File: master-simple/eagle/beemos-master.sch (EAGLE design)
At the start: 56 parts, among them CON1 BATTERY, CON2 JACK_DC_BARREL, CON3 SPI, IC1 32U4, IC2 MCP73831T, IC3 MCP1703CB, IC4 DMP1045U, J1 RJ12STRAIGHT-I2C, J2 RJ12STRAIGHT-I2C, J3 RJ12STRAIGHT-I2C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

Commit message: master: cleanup
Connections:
- net N$7: now also IC2.STAT
- net SCL: no longer R1.1
- net SDA: now also R1.1
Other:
- moved on the sheet: R1, R6
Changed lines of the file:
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@@
 <?xml version="1.0" encoding="utf-8"?>
 <!DOCTYPE eagle SYSTEM "eagle.dtd">
-<eagle version="9.0.0">
+<eagle version="8.7.1">
 <drawing>
 <settings>
@@
 <instance part="GND7" gate="1" x="45.72" y="167.64" rot="R180"/>
 <instance part="P+2" gate="G$1" x="73.66" y="215.9"/>
-<instance part="R1" gate="G$1" x="185.42" y="147.32" rot="R90"/>
-<instance part="R6" gate="G$1" x="193.04" y="147.32" rot="R90"/>
+<instance part="R1" gate="G$1" x="185.42" y="152.4" rot="R90"/>
+<instance part="R6" gate="G$1" x="193.04" y="152.4" rot="R90"/>
 <instance part="P+3" gate="G$1" x="96.52" y="200.66"/>
 <instance part="P+4" gate="G$1" x="106.68" y="205.74"/>
@@
 <attribute name="ELECROW" x="66.04" y="91.44" size="1.778" layer="96" display="off"/>
 </instance>
-<instance part="SUPPLY1" gate="G$1" x="195.58" y="157.48"/>
+<instance part="SUPPLY1" gate="G$1" x="195.58" y="162.56"/>
 <instance part="GND3" gate="1" x="238.76" y="86.36" rot="R270"/>
 <instance part="RT2" gate="G$1" x="236.22" y="96.52" rot="R180"/>
@@
 <wire x1="160.02" y1="208.28" x2="175.26" y2="208.28" width="0.1524" layer="91"/>
 <label x="170.18" y="208.28" size="1.778" layer="95"/>
+<junction x="160.02" y="208.28"/>
 </segment>
 </net>
@@
 <wire x1="160.02" y1="210.82" x2="175.26" y2="210.82" width="0.1524" layer="91"/>
 <label x="170.18" y="210.82" size="1.778" layer="95"/>
+<junction x="160.02" y="210.82"/>
 </segment>
 </net>
@@
 <wire x1="160.02" y1="213.36" x2="175.26" y2="213.36" width="0.1524" layer="91"/>
 <label x="170.18" y="213.36" size="1.778" layer="95"/>
+<junction x="160.02" y="213.36"/>
 </segment>
 </net>
@@
 <wire x1="160.02" y1="215.9" x2="175.26" y2="215.9" width="0.1524" layer="91"/>
 <label x="170.18" y="215.9" size="1.778" layer="95"/>
+<junction x="160.02" y="215.9"/>
 </segment>
 <segment>
@@
 <wire x1="160.02" y1="205.74" x2="175.26" y2="205.74" width="0.1524" layer="91"/>
 <label x="170.18" y="205.74" size="1.778" layer="95"/>
+<junction x="160.02" y="205.74"/>
 </segment>
 </net>
@@
 <segment>
 <pinref part="IC1" gate="G$1" pin="PD1(INT1/SDA)"/>
-<wire x1="160.02" y1="144.78" x2="175.26" y2="144.78" width="0.1524" layer="91"/>
+<wire x1="160.02" y1="144.78" x2="185.42" y2="144.78" width="0.1524" layer="91"/>
 <label x="170.18" y="144.78" size="1.778" layer="95"/>
+<pinref part="R1" gate="G$1" pin="1"/>
+<wire x1="185.42" y1="147.32" x2="185.42" y2="144.78" width="0.1524" layer="91"/>
 </segment>
 <segment>
@@
 <net name="SCL" class="0">
 <segment>
-<pinref part="IC1" gate="G$1" pin="PD0(INT0/OC0B/SCL)"/>
-<wire x1="160.02" y1="142.24" x2="185.42" y2="142.24" width="0.1524" layer="91"/>
-<label x="170.18" y="142.24" size="1.778" layer="95"/>
-<pinref part="R1" gate="G$1" pin="1"/>
-<pinref part="R6" gate="G$1" pin="1"/>
-<wire x1="193.04" y1="142.24" x2="185.42" y2="142.24" width="0.1524" layer="91"/>
-<junction x="185.42" y="142.24"/>
-</segment>
-<segment>
 <pinref part="U$1" gate="G$1" pin="SCL"/>
 <wire x1="27.94" y1="162.56" x2="45.72" y2="162.56" width="0.1524" layer="91"/>
@@
 <label x="91.44" y="27.94" size="1.778" layer="95"/>
 </segment>
+<segment>
+<pinref part="IC1" gate="G$1" pin="PD0(INT0/OC0B/SCL)"/>
+<pinref part="R6" gate="G$1" pin="1"/>
+<wire x1="160.02" y1="142.24" x2="193.04" y2="142.24" width="0.1524" layer="91"/>
+<wire x1="193.04" y1="142.24" x2="193.04" y2="147.32" width="0.1524" layer="91"/>
+<label x="170.18" y="142.24" size="1.778" layer="95"/>
+</segment>
 </net>
 <net name="TX" class="0">
@@
 <wire x1="160.02" y1="195.58" x2="175.26" y2="195.58" width="0.1524" layer="91"/>
 <label x="170.18" y="195.58" size="1.778" layer="95"/>
+<junction x="160.02" y="195.58"/>
 </segment>
 <segment>
@@
 <wire x1="160.02" y1="203.2" x2="175.26" y2="203.2" width="0.1524" layer="91"/>
 <label x="170.18" y="203.2" size="1.778" layer="95"/>
+<junction x="160.02" y="203.2"/>
 </segment>
 </net>
@@
 <wire x1="160.02" y1="198.12" x2="175.26" y2="198.12" width="0.1524" layer="91"/>
 <label x="170.18" y="198.12" size="1.778" layer="95"/>
+<junction x="160.02" y="198.12"/>
 </segment>
 </net>
@@
 <pinref part="R1" gate="G$1" pin="2"/>
 <pinref part="R6" gate="G$1" pin="2"/>
-<wire x1="185.42" y1="152.4" x2="193.04" y2="152.4" width="0.1524" layer="91"/>
-<wire x1="193.04" y1="152.4" x2="195.58" y2="152.4" width="0.1524" layer="91"/>
+<wire x1="185.42" y1="157.48" x2="193.04" y2="157.48" width="0.1524" layer="91"/>
+<wire x1="193.04" y1="157.48" x2="195.58" y2="157.48" width="0.1524" layer="91"/>
 <pinref part="SUPPLY1" gate="G$1" pin="VDD"/>
-<wire x1="195.58" y1="154.94" x2="195.58" y2="152.4" width="0.1524" layer="91"/>
-<junction x="193.04" y="152.4"/>
+<wire x1="195.58" y1="160.02" x2="195.58" y2="157.48" width="0.1524" layer="91"/>
+<junction x="193.04" y="157.48"/>
 </segment>
 </net>
@@
 <pinref part="R16" gate="G$1" pin="2"/>
 <wire x1="71.12" y1="91.44" x2="73.66" y2="91.44" width="0.1524" layer="91"/>
-</segment>
-</net>
+<pinref part="IC2" gate="G$1" pin="STAT"/>
+<junction x="73.66" y="91.44"/>
+</segment>
+</net>

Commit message: Arranged labels and resistors in beemos master board layout
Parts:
- D4: value ||Schottky -> Schottky||
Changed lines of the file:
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@@
 <?xml version="1.0" encoding="utf-8"?>
 <!DOCTYPE eagle SYSTEM "eagle.dtd">
-<eagle version="8.7.1">
+<eagle version="9.0.0">
 <drawing>
 <settings>
@@
 <part name="J4" library="lpatiny" deviceset="RJ12" device="STRAIGHT-I2C" value="RJ12STRAIGHT-I2C"/>
 <part name="CON2" library="lpatiny" deviceset="JACK_DC_BARREL" device=""/>
-<part name="D4" library="diode" library_urn="urn:adsk.eagle:library:210" deviceset="MBR0520LT" device="" package3d_urn="urn:adsk.eagle:package:43420/1" value="||Schottky">
+<part name="D4" library="diode" library_urn="urn:adsk.eagle:library:210" deviceset="MBR0520LT" device="" package3d_urn="urn:adsk.eagle:package:43420/1" value="Schottky||">
 <attribute name="LCSC" value="C82544"/>
 <attribute name="MPN" value="621-1N5819HW-F"/>

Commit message: Added power/com LEDs, extra pins exposed, cristal symmetric
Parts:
- added LED1: red, led:LEDCHIP-LED0805
- added LED2: white, led:LEDCHIP-LED0805
- added R17, R20: 10k, rcl:R-EU_R0805
- added X6: 22-23-2081, con-molex:22-23-2081
- C1, C2: value 18pF -> 22pF
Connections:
- new net N$10: LED1.A, R17.1
- new net N$11: LED2.A, R20.1
- net 3.3V: now also R17.2, X6-7.S
- net A0: now also X6-5.S
- net A1: now also X6-4.S
- net A2: now also X6-3.S
- net A3: now also X6-2.S
- net D13: now also R20.2
- net D5: now also X6-6.S
- net GND: now also LED1.C, LED2.C, X6-1.S
- net VBAT1: now also X6-8.S
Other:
- note added: "Extra pins"
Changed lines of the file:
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@@
 <?xml version="1.0" encoding="utf-8"?>
 <!DOCTYPE eagle SYSTEM "eagle.dtd">
-<eagle version="9.0.0">
+<eagle version="8.7.1">
 <drawing>
 <settings>
@@
 <attribute name="MPN" value="556-ATMEGA32U4RC-AU"/>
 </part>
-<part name="C1" library="rcl" library_urn="urn:adsk.eagle:library:334" deviceset="C-EU" device="C0805K" package3d_urn="urn:adsk.eagle:package:23681/2" value="18pF">
+<part name="C1" library="rcl" library_urn="urn:adsk.eagle:library:334" deviceset="C-EU" device="C0805K" package3d_urn="urn:adsk.eagle:package:23681/2" value="22pF">
 <spice>
 <pinmapping spiceprefix="C">
@@
 <attribute name="MPN" value="77-VJ1206A180JXXPBC"/>
 </part>
-<part name="C2" library="rcl" library_urn="urn:adsk.eagle:library:334" deviceset="C-EU" device="C0805K" package3d_urn="urn:adsk.eagle:package:23681/2" value="18pF">
+<part name="C2" library="rcl" library_urn="urn:adsk.eagle:library:334" deviceset="C-EU" device="C0805K" package3d_urn="urn:adsk.eagle:package:23681/2" value="22pF">
 <spice>
 <pinmapping spiceprefix="C">
@@
 <part name="R10" library="rcl" deviceset="R-EU_" device="R0805" value="100"/>
 <part name="JP1" library="SparkFun" deviceset="M06" device="RA"/>
+<part name="X6" library="con-molex" library_urn="urn:adsk.eagle:library:165" deviceset="22-23-2081" device=""/>
+<part name="R17" library="rcl" library_urn="urn:adsk.eagle:library:334" deviceset="R-EU_" device="R0805" package3d_urn="urn:adsk.eagle:package:23553/2" value="10k">
+<spice>
+<pinmapping spiceprefix="R">
+<pinmap gate="G$1" pin="1" pinorder="1"/>
+<pinmap gate="G$1" pin="2" pinorder="2"/>
+</pinmapping>
+</spice>
+</part>
+<part name="LED1" library="led" library_urn="urn:adsk.eagle:library:259" deviceset="LED" device="CHIP-LED0805" package3d_urn="urn:adsk.eagle:package:15818/2" value="red"/>
+<part name="P+7" library="SparkFun" deviceset="3.3V" device=""/>
+<part name="GND4" library="supply1" deviceset="GND" device=""/>
+<part name="R20" library="rcl" library_urn="urn:adsk.eagle:library:334" deviceset="R-EU_" device="R0805" package3d_urn="urn:adsk.eagle:package:23553/2" value="10k"/>
+<part name="LED2" library="led" library_urn="urn:adsk.eagle:library:259" deviceset="LED" device="CHIP-LED0805" package3d_urn="urn:adsk.eagle:package:15818/2" value="white"/>
+<part name="GND6" library="supply1" deviceset="GND" device=""/>
 </parts>
 <sheets>
@@
 <wire x1="142.24" y1="7.62" x2="142.24" y2="68.58" width="1.27" layer="94"/>
 <wire x1="142.24" y1="68.58" x2="292.1" y2="68.58" width="1.27" layer="94"/>
+<text x="210.82" y="60.96" size="5.08" layer="91">Extra pins</text>
 </plain>
 <instances>
@@
 <instance part="R10" gate="G$1" x="246.38" y="101.6" rot="MR90"/>
 <instance part="JP1" gate="G$1" x="170.18" y="35.56" rot="R180"/>
+<instance part="X6" gate="-1" x="223.52" y="45.72"/>
+<instance part="X6" gate="-2" x="223.52" y="43.18"/>
+<instance part="X6" gate="-3" x="223.52" y="40.64"/>
+<instance part="X6" gate="-4" x="223.52" y="38.1"/>
+<instance part="X6" gate="-5" x="223.52" y="35.56"/>
+<instance part="X6" gate="-6" x="223.52" y="33.02"/>
+<instance part="X6" gate="-7" x="223.52" y="30.48"/>
+<instance part="X6" gate="-8" x="223.52" y="27.94"/>
+<instance part="R17" gate="G$1" x="259.08" y="35.56" rot="R90"/>
+<instance part="LED1" gate="G$1" x="259.08" y="25.4"/>
+<instance part="P+7" gate="G$1" x="259.08" y="43.18"/>
+<instance part="GND4" gate="1" x="259.08" y="15.24"/>
+<instance part="R20" gate="G$1" x="274.32" y="35.56" rot="R90"/>
+<instance part="LED2" gate="G$1" x="274.32" y="25.4"/>
+<instance part="GND6" gate="1" x="274.32" y="15.24"/>
 </instances>
 <busses>
@@
 <label x="160.02" y="27.94" size="1.778" layer="95"/>
 </segment>
+<segment>
+<pinref part="X6" gate="-1" pin="S"/>
+<wire x1="220.98" y1="45.72" x2="218.44" y2="45.72" width="0.1524" layer="91"/>
+<label x="215.9" y="45.72" size="1.778" layer="95"/>
+</segment>
+<segment>
+<pinref part="LED1" gate="G$1" pin="C"/>
+<pinref part="GND4" gate="1" pin="GND"/>
+<wire x1="259.08" y1="20.32" x2="259.08" y2="17.78" width="0.1524" layer="91"/>
+</segment>
+<segment>
+<pinref part="LED2" gate="G$1" pin="C"/>
+<pinref part="GND6" gate="1" pin="GND"/>
+<wire x1="274.32" y1="20.32" x2="274.32" y2="17.78" width="0.1524" layer="91"/>
+</segment>
 </net>
 <net name="SCK" class="0">
@@
 <junction x="160.02" y="208.28"/>
 </segment>
+<segment>
+<pinref part="X6" gate="-3" pin="S"/>
+<wire x1="220.98" y1="40.64" x2="218.44" y2="40.64" width="0.1524" layer="91"/>
+<label x="215.9" y="40.64" size="1.778" layer="95"/>
+</segment>
 </net>
 <net name="A3" class="0">
@@
 <label x="170.18" y="210.82" size="1.778" layer="95"/>
 <junction x="160.02" y="210.82"/>
+</segment>
+<segment>
+<pinref part="X6" gate="-2" pin="S"/>
+<wire x1="220.98" y1="43.18" x2="218.44" y2="43.18" width="0.1524" layer="91"/>
+<label x="215.9" y="43.18" size="1.778" layer="95"/>
 </segment>
 </net>
@@
 <junction x="160.02" y="205.74"/>
 </segment>
+<segment>
+<pinref part="X6" gate="-4" pin="S"/>
+<wire x1="220.98" y1="38.1" x2="218.44" y2="38.1" width="0.1524" layer="91"/>
+<label x="215.9" y="38.1" size="1.778" layer="95"/>
+</segment>
 </net>
 <net name="D5" class="0">
@@
 <wire x1="160.02" y1="190.5" x2="175.26" y2="190.5" width="0.1524" layer="91"/>
 <label x="170.18" y="190.5" size="1.778" layer="95"/>
+</segment>
+<segment>
+<pinref part="X6" gate="-6" pin="S"/>
+<wire x1="220.98" y1="33.02" x2="218.44" y2="33.02" width="0.1524" layer="91"/>
+<label x="215.9" y="33.02" size="1.778" layer="95"/>
 </segment>
 </net>
@@
 <label x="170.18" y="203.2" size="1.778" layer="95"/>
 <junction x="160.02" y="203.2"/>
+</segment>
+<segment>
+<pinref part="X6" gate="-5" pin="S"/>
+<wire x1="220.98" y1="35.56" x2="218.44" y2="35.56" width="0.1524" layer="91"/>
+<label x="215.9" y="35.56" size="1.778" layer="95"/>
 </segment>
 </net>
@@
 <label x="157.48" y="38.1" size="1.778" layer="95"/>
 </segment>
+<segment>
+<pinref part="X6" gate="-8" pin="S"/>
+<wire x1="220.98" y1="27.94" x2="218.44" y2="27.94" width="0.1524" layer="91"/>
+<label x="215.9" y="27.94" size="1.778" layer="95"/>
+</segment>
 </net>
 <net name="N$6" class="0">
@@
 <wire x1="160.02" y1="187.96" x2="175.26" y2="187.96" width="0.1524" layer="91"/>
 <label x="170.18" y="187.96" size="1.778" layer="95"/>
+</segment>
+<segment>
+<pinref part="R20" gate="G$1" pin="2"/>
+<wire x1="274.32" y1="40.64" x2="274.32" y2="43.18" width="0.1524" layer="91"/>
+<label x="274.32" y="43.18" size="1.778" layer="95"/>
 </segment>
 </net>
@@
 <pinref part="P+6" gate="G$1" pin="3.3V"/>
 <wire x1="246.38" y1="109.22" x2="246.38" y2="106.68" width="0.1524" layer="91"/>
+</segment>
+<segment>
+<pinref part="X6" gate="-7" pin="S"/>
+<wire x1="220.98" y1="30.48" x2="218.44" y2="30.48" width="0.1524" layer="91"/>
+<label x="215.9" y="30.48" size="1.778" layer="95"/>
+</segment>
+<segment>
+<pinref part="R17" gate="G$1" pin="2"/>
+<pinref part="P+7" gate="G$1" pin="3.3V"/>
+<wire x1="259.08" y1="40.64" x2="259.08" y2="43.18" width="0.1524" layer="91"/>
 </segment>
 </net>
@@
 </segment>
 </net>
+<net name="N$10" class="0">
+<segment>
+<pinref part="LED1" gate="G$1" pin="A"/>
+<pinref part="R17" gate="G$1" pin="1"/>
+<wire x1="259.08" y1="27.94" x2="259.08" y2="30.48" width="0.1524" layer="91"/>
+</segment>
+</net>
+<net name="N$11" class="0">
+<segment>
+<pinref part="LED2" gate="G$1" pin="A"/>
+<pinref part="R20" gate="G$1" pin="1"/>
+<wire x1="274.32" y1="27.94" x2="274.32" y2="30.48" width="0.1524" layer="91"/>
+</segment>
+</net>

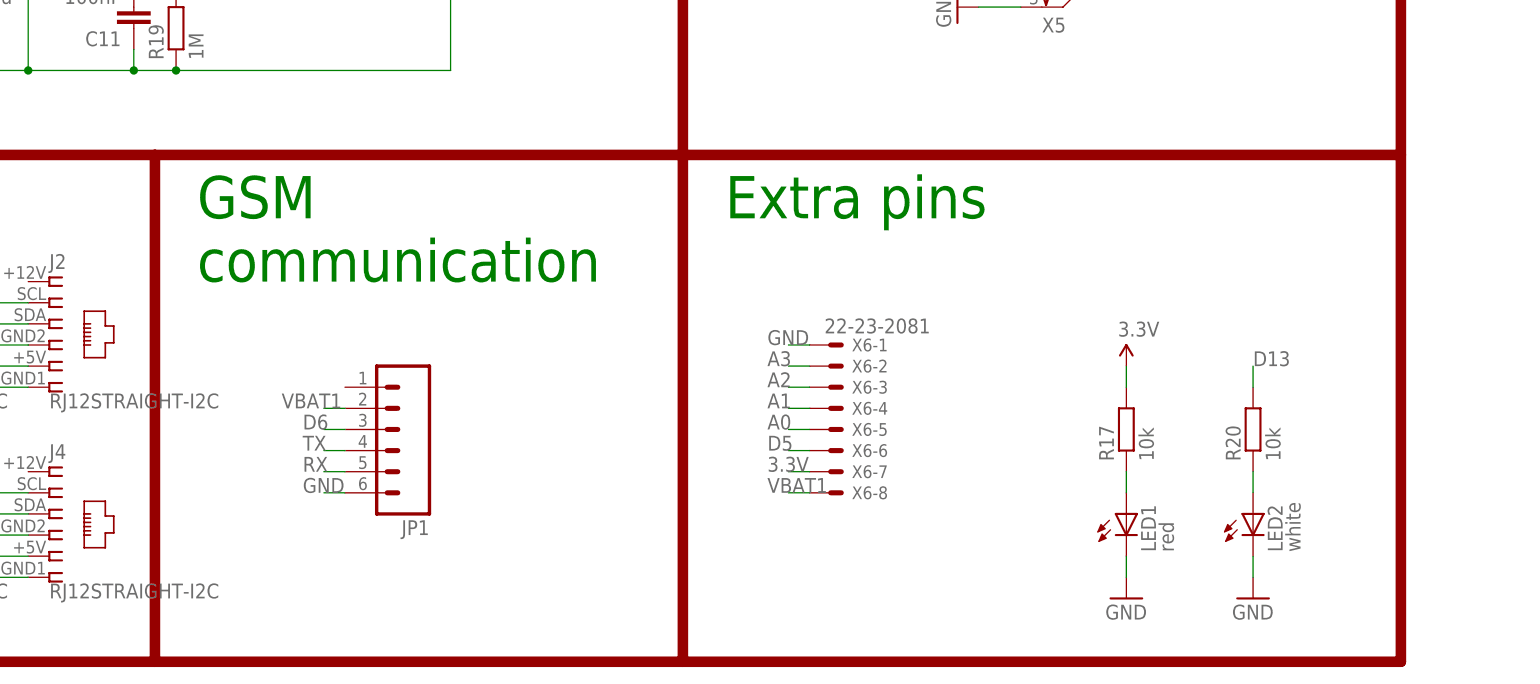
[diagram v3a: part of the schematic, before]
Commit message: Updated schematic with LEDs
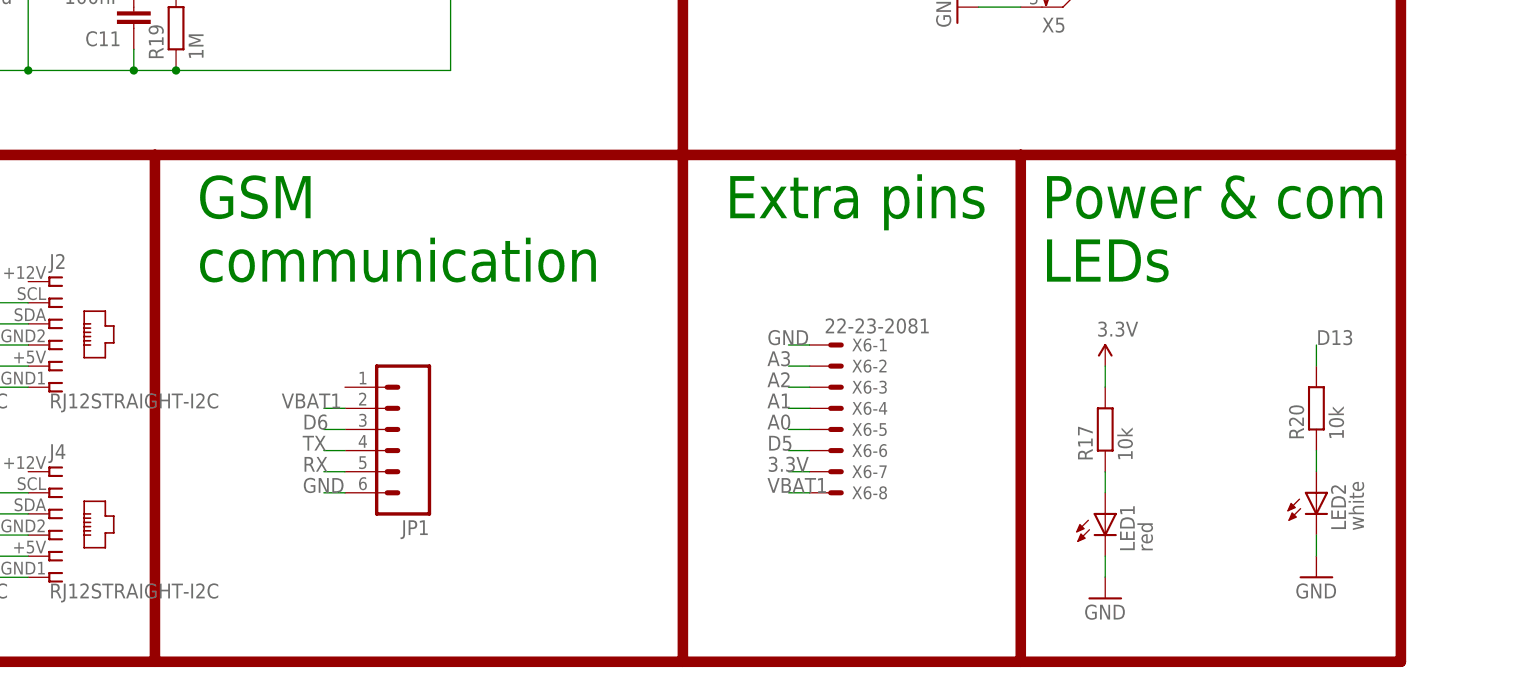
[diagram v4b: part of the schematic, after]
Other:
- note added: "Power & com LEDs"
- moved on the sheet: LED1, LED2, R17, R20
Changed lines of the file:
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@@
 <text x="0" y="187.96" size="5.08" layer="91">MEMORY</text>
 <wire x1="205.74" y1="233.68" x2="292.1" y2="233.68" width="1.27" layer="94"/>
-<wire x1="205.74" y1="7.62" x2="292.1" y2="7.62" width="1.27" layer="94"/>
+<wire x1="205.74" y1="7.62" x2="246.38" y2="7.62" width="1.27" layer="94"/>
+<wire x1="246.38" y1="7.62" x2="292.1" y2="7.62" width="1.27" layer="94"/>
 <wire x1="292.1" y1="7.62" x2="292.1" y2="129.54" width="1.27" layer="94"/>
 <wire x1="292.1" y1="129.54" x2="292.1" y2="233.68" width="1.27" layer="94"/>
@@
 <text x="213.36" y="119.38" size="5.08" layer="91">Humidity</text>
 <wire x1="142.24" y1="7.62" x2="142.24" y2="68.58" width="1.27" layer="94"/>
-<wire x1="142.24" y1="68.58" x2="292.1" y2="68.58" width="1.27" layer="94"/>
+<wire x1="142.24" y1="68.58" x2="246.38" y2="68.58" width="1.27" layer="94"/>
 <text x="210.82" y="60.96" size="5.08" layer="91">Extra pins</text>
+<wire x1="246.38" y1="68.58" x2="292.1" y2="68.58" width="1.27" layer="94"/>
+<wire x1="246.38" y1="7.62" x2="246.38" y2="68.58" width="1.27" layer="94"/>
+<text x="248.92" y="53.34" size="5.08" layer="91">Power &amp; com
+LEDs</text>
 </plain>
 <instances>
@@
 <instance part="X6" gate="-7" x="223.52" y="30.48"/>
 <instance part="X6" gate="-8" x="223.52" y="27.94"/>
-<instance part="R17" gate="G$1" x="259.08" y="35.56" rot="R90"/>
-<instance part="LED1" gate="G$1" x="259.08" y="25.4"/>
-<instance part="P+7" gate="G$1" x="259.08" y="43.18"/>
-<instance part="GND4" gate="1" x="259.08" y="15.24"/>
-<instance part="R20" gate="G$1" x="274.32" y="35.56" rot="R90"/>
-<instance part="LED2" gate="G$1" x="274.32" y="25.4"/>
-<instance part="GND6" gate="1" x="274.32" y="15.24"/>
+<instance part="R17" gate="G$1" x="256.54" y="35.56" rot="R90"/>
+<instance part="LED1" gate="G$1" x="256.54" y="25.4"/>
+<instance part="P+7" gate="G$1" x="256.54" y="43.18"/>
+<instance part="GND4" gate="1" x="256.54" y="15.24"/>
+<instance part="R20" gate="G$1" x="281.94" y="38.1" rot="R90"/>
+<instance part="LED2" gate="G$1" x="281.94" y="27.94"/>
+<instance part="GND6" gate="1" x="281.94" y="17.78"/>
 </instances>
 <busses>
@@
 <pinref part="LED1" gate="G$1" pin="C"/>
 <pinref part="GND4" gate="1" pin="GND"/>
-<wire x1="259.08" y1="20.32" x2="259.08" y2="17.78" width="0.1524" layer="91"/>
+<wire x1="256.54" y1="20.32" x2="256.54" y2="17.78" width="0.1524" layer="91"/>
 </segment>
 <segment>
 <pinref part="LED2" gate="G$1" pin="C"/>
 <pinref part="GND6" gate="1" pin="GND"/>
-<wire x1="274.32" y1="20.32" x2="274.32" y2="17.78" width="0.1524" layer="91"/>
+<wire x1="281.94" y1="22.86" x2="281.94" y2="20.32" width="0.1524" layer="91"/>
 </segment>
 </net>
@@
 <segment>
 <pinref part="R20" gate="G$1" pin="2"/>
-<wire x1="274.32" y1="40.64" x2="274.32" y2="43.18" width="0.1524" layer="91"/>
-<label x="274.32" y="43.18" size="1.778" layer="95"/>
+<wire x1="281.94" y1="43.18" x2="281.94" y2="45.72" width="0.1524" layer="91"/>
+<label x="281.94" y="45.72" size="1.778" layer="95"/>
 </segment>
 </net>
@@
 <pinref part="R17" gate="G$1" pin="2"/>
 <pinref part="P+7" gate="G$1" pin="3.3V"/>
-<wire x1="259.08" y1="40.64" x2="259.08" y2="43.18" width="0.1524" layer="91"/>
+<wire x1="256.54" y1="40.64" x2="256.54" y2="43.18" width="0.1524" layer="91"/>
 </segment>
 </net>
@@
 <pinref part="LED1" gate="G$1" pin="A"/>
 <pinref part="R17" gate="G$1" pin="1"/>
-<wire x1="259.08" y1="27.94" x2="259.08" y2="30.48" width="0.1524" layer="91"/>
+<wire x1="256.54" y1="27.94" x2="256.54" y2="30.48" width="0.1524" layer="91"/>
 </segment>
 </net>
@@
 <pinref part="LED2" gate="G$1" pin="A"/>
 <pinref part="R20" gate="G$1" pin="1"/>
-<wire x1="274.32" y1="27.94" x2="274.32" y2="30.48" width="0.1524" layer="91"/>
-</segment>
-</net>
+<wire x1="281.94" y1="30.48" x2="281.94" y2="33.02" width="0.1524" layer="91"/>
+</segment>
+</net>
